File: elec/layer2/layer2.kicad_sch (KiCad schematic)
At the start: 49 parts, among them J1 Conn_01x03, J10 Conn_01x05, J12 XT60-M, J17 Conn_01x02, J18 Conn_01x02, J19 XT30UPB-M, J2 XT30UPB-M, J3 Conn_01x04, J4 Conn_01x05, J5 Conn_01x03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

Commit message: l3 almost done
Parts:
- added J8: XT30PW-M, layer2-pcb-footprints:AMASS_XT30PW-M, symbol layer1-pcb-symbols:XT30PW-M
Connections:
- net +5V: now also J8.P
- net GND: now also J8.N
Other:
- moved on the sheet: J9

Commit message: prod: l2, l3
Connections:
- net RX (L3-Teensy) renamed RX (L3-ESP32)
- net TX (L3-Teensy) renamed TX (L3-ESP32)
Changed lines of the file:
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@@
 		)
 	)
-	(label "TX (L3-Teensy)"
+	(label "TX (L3-ESP32)"
 		(at 271.78 60.96 180)
 		(effects
@@
 		)
 	)
-	(label "RX (L3-Teensy)"
+	(label "RX (L3-ESP32)"
 		(at 271.78 63.5 180)
 		(effects
@@
 		)
 	)
-	(label "RX (L3-Teensy)"
+	(label "RX (L3-ESP32)"
 		(at 320.04 76.2 0)
 		(effects
@@
 		)
 	)
-	(label "TX (L3-Teensy)"
+	(label "TX (L3-ESP32)"
 		(at 320.04 78.74 0)
 		(effects

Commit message: l3 : sw change
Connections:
- net GND: now also SW1.1 (B); no longer SW1.2 (C)
- net Motors Enable: now also SW1.2 (C); no longer SW1.1 (B)
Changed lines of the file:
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@@
 	)
 	(label "Motors Enable"
-		(at 250.19 142.24 0)
+		(at 285.75 146.05 0)
 		(effects
 			(font
@@
 	(symbol
 		(lib_id "power:GND")
-		(at 285.75 146.05 0)
+		(at 250.19 142.24 0)
 		(unit 1)
 		(exclude_from_sim no)
@@
 		(dnp no)
 		(property "Reference" "#PWR014"
-			(at 285.75 152.4 0)
+			(at 250.19 148.59 0)
 			(effects
 				(font
@@
 		)
 		(property "Value" "GND"
-			(at 285.75 150.622 0)
+			(at 250.19 146.812 0)
 			(effects
 				(font
@@
 		)
 		(property "Footprint" ""
-			(at 285.75 146.05 0)
+			(at 250.19 142.24 0)
 			(effects
 				(font
@@
 		)
 		(property "Datasheet" ""
-			(at 285.75 146.05 0)
+			(at 250.19 142.24 0)
 			(effects
 				(font
@@
 		)
 		(property "Description" "Power symbol creates a global label with name \"GND\" , ground"
-			(at 285.75 146.05 0)
-			(effects
-				(font
+			(at 250.19 142.24 0)
+			(effects
+				(font

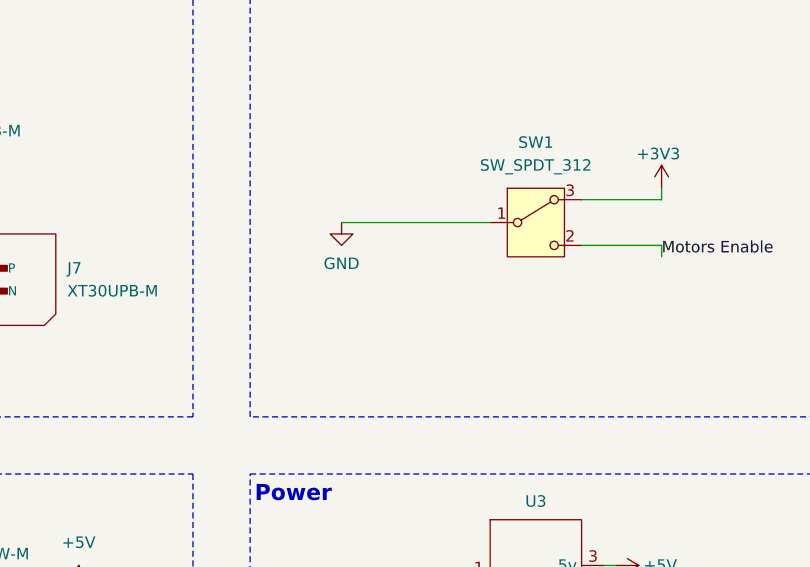
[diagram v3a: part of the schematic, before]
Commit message: fixed enable pull dowj
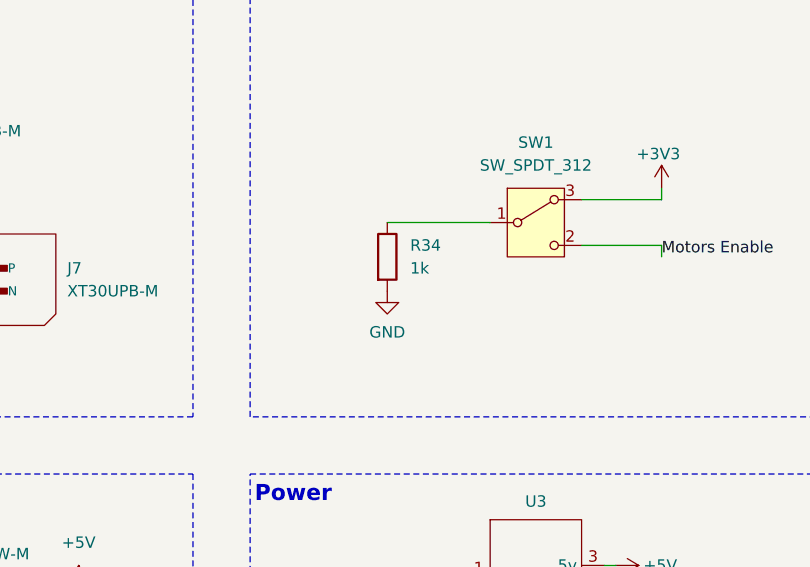
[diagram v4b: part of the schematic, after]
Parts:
- added R34: 1k, Resistor_SMD:R_0603_1608Metric, symbol Device:R
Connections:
- net GND: now also R34.2; no longer SW1.1 (B)
- new net: R34.1, SW1.1 (B)
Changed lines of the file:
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@@
 	(wire
 		(pts
-			(xy 250.19 142.24) (xy 266.7 142.24)
+			(xy 271.78 190.5) (xy 271.78 191.77)
 		)
 		(stroke
@@
 	(wire
 		(pts
-			(xy 271.78 190.5) (xy 271.78 191.77)
+			(xy 255.27 142.24) (xy 266.7 142.24)
 		)
 		(stroke
@@
 				(path "/df41387d-f005-440e-9787-7a1b7b7bf447"
 					(reference "#PWR013")
+					(unit 1)
+				)
+			)
+		)
+	)
+	(symbol
+		(lib_id "Device:R")
+		(at 255.27 146.05 0)
+		(unit 1)
+		(exclude_from_sim no)
+		(in_bom yes)
+		(on_board yes)
+		(dnp no)
+		(fields_autoplaced yes)
+		(property "Reference" "R34"
+			(at 257.81 144.7799 0)
+			(effects
+				(font
+					(size 1.27 1.27)
+				)
+				(justify left)
+			)
+		)
+		(property "Value" "1k"
+			(at 257.81 147.3199 0)
+			(effects
+				(font
+					(size 1.27 1.27)
+				)
+				(justify left)
+			)
+		)
+		(property "Footprint" "Resistor_SMD:R_0603_1608Metric"
+			(at 253.492 146.05 90)
+			(effects
+				(font
+					(size 1.27 1.27)
+				)
+				(hide yes)
+			)
+		)
+		(property "Datasheet" "~"
+			(at 255.27 146.05 0)
+			(effects
+				(font
+					(size 1.27 1.27)
+				)
+				(hide yes)
+			)
+		)
+		(property "Description" "Resistor"
+			(at 255.27 146.05 0)
+			(effects
+				(font
+					(size 1.27 1.27)
+				)
+				(hide yes)
+			)
+		)
+		(pin "2"
+		)
+		(pin "1"
+		)
+		(instances
+			(project "layer2"
+				(path "/df41387d-f005-440e-9787-7a1b7b7bf447"
+					(reference "R34")
 					(unit 1)
 				)
@@
 	(symbol
 		(lib_id "power:GND")
-		(at 250.19 142.24 0)
+		(at 255.27 149.86 0)
 		(unit 1)
 		(exclude_from_sim no)
@@
 		(dnp no)
 		(property "Reference" "#PWR014"
-			(at 250.19 148.59 0)
+			(at 255.27 156.21 0)
 			(effects
 				(font
@@
 		)
 		(property "Value" "GND"
-			(at 250.19 146.812 0)
+			(at 255.27 154.432 0)
 			(effects
 				(font
@@
 		)
 		(property "Footprint" ""
-			(at 250.19 142.24 0)
+			(at 255.27 149.86 0)
 			(effects
 				(font
@@
 		)
 		(property "Datasheet" ""
-			(at 250.19 142.24 0)
+			(at 255.27 149.86 0)
 			(effects
 				(font
@@
 		)
 		(property "Description" "Power symbol creates a global label with name \"GND\" , ground"
-			(at 250.19 142.24 0)
-			(effects
-				(font
+			(at 255.27 149.86 0)
+			(effects
+				(font

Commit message: l2 done
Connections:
- net RX (L1-Teensy): now also J3.3 (Pin_3); no longer J3.2 (Pin_2)
- net RX (L3-Cam: now also J4.4 (Pin_4); no longer J4.3 (Pin_3)
- net RX (L3-ESP32): now also J4.2 (Pin_2); no longer J4.1 (Pin_1)
- net TX (L1-Teensy): now also J3.2 (Pin_2); no longer J3.3 (Pin_3)
- net TX (L3-Cam): now also J4.3 (Pin_3); no longer J4.4 (Pin_4)
- net TX (L3-ESP32): now also J4.1 (Pin_1); no longer J4.2 (Pin_2)
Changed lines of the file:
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@@
 	)
 	(label "TX (L1-Teensy)"
-		(at 318.77 55.88 0)
+		(at 318.77 53.34 0)
 		(effects
 			(font
@@
 	)
 	(label "RX (L3-ESP32)"
-		(at 320.04 76.2 0)
+		(at 320.04 78.74 0)
 		(effects
 			(font
@@
 	)
 	(label "TX (L3-Cam)"
-		(at 320.04 83.82 0)
+		(at 320.04 81.28 0)
 		(effects
 			(font
@@
 	)
 	(label "RX (L3-Cam"
-		(at 320.04 81.28 0)
+		(at 320.04 83.82 0)
 		(effects
 			(font
@@
 	)
 	(label "RX (L1-Teensy)"
-		(at 318.77 53.34 0)
+		(at 318.77 55.88 0)
 		(effects
 			(font
@@
 	)
 	(label "TX (L3-ESP32)"
-		(at 320.04 78.74 0)
-		(effects
-			(font
+		(at 320.04 76.2 0)
+		(effects
+			(font

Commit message: chore: fix all 3 layers; prod: all 3 layers
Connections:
- net RX (L3-ESP32): now also TP16.1, U1.21; no longer TP17.1, U1.20
- net TX (L3-Cam): now also TP23.1, U1.14; no longer TP22.1, U1.15
- net TX (L3-ESP32): now also TP17.1, U1.20; no longer TP16.1, U1.21
- removed net RX (L3-Cam: J4.4 (Pin_4), TP23.1, U1.14
- new net RX (L3-Cam): J4.4 (Pin_4), TP22.1, U1.15
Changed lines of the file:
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@@
 	)
 	(label "TX (L3-ESP32)"
-		(at 271.78 60.96 180)
+		(at 271.78 63.5 180)
 		(effects
 			(font
@@
 		)
 	)
-	(label "RX (L3-Cam"
-		(at 271.78 78.74 180)
+	(label "RX (L3-Cam)"
+		(at 271.78 76.2 180)
 		(effects
 			(font
@@
 	)
 	(label "RX (L3-ESP32)"
-		(at 271.78 63.5 180)
+		(at 271.78 60.96 180)
 		(effects
 			(font
@@
 		)
 	)
-	(label "RX (L3-Cam"
+	(label "RX (L3-Cam)"
 		(at 320.04 83.82 0)
 		(effects
@@
 	)
 	(label "TX (L3-Cam)"
-		(at 271.78 76.2 180)
-		(effects
-			(font
+		(at 271.78 78.74 180)
+		(effects
+			(font
